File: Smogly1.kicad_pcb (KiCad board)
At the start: 2 copper layers, 93.2 x 68 mm, 9 parts, among them J1 VCC IN, J10 NodeMCU A0-VIN, J11 NodeMCU D0-3.3V, J2 PMSx003, J3 BME280, J4 microUSB, J5 5/3.3/GND, J6 DeepSleep, J8 D5/6/7/8

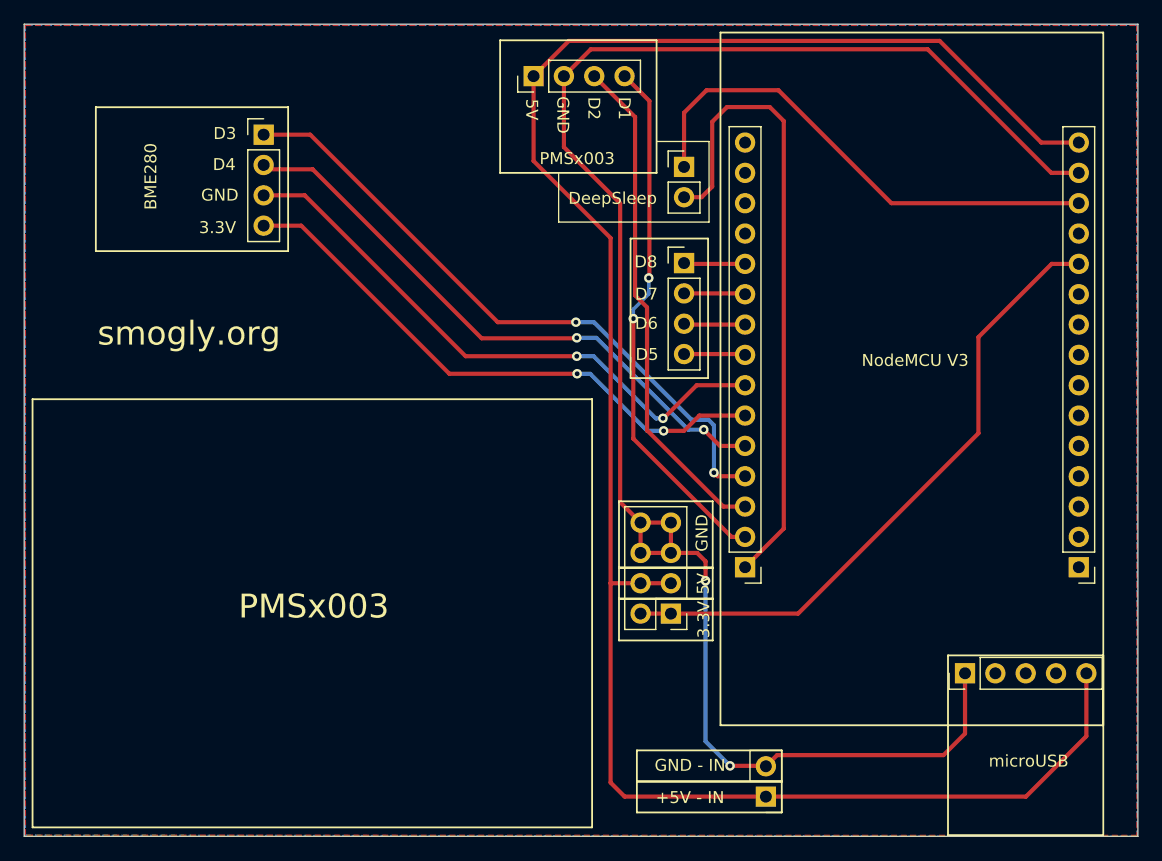
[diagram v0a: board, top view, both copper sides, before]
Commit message: added PMS7003 connector
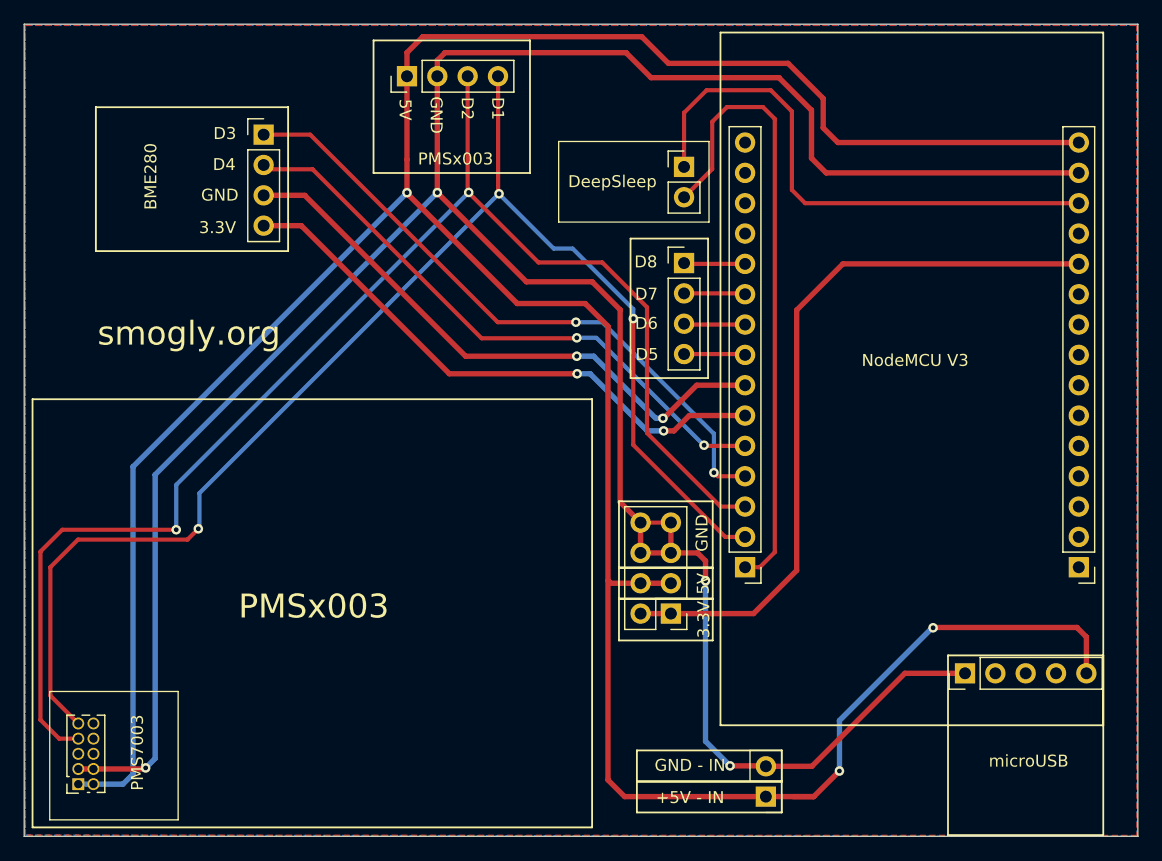
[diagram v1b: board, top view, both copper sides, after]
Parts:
- added J9: PMS7003_Conn, Connector_PinSocket_1.27mm:PinSocket_2x05_P1.27mm_Vertical, F.Cu at (169.5, 132.1)
- moved J2 10.6 mm to (197.0, 72.8)
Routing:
- net +5V: track 165.0 -> 255.8 mm, vias 0 -> 3
- net GND: track 145.6 -> 228.4 mm, vias 2 -> 4
- net Net-(J11-Pad3): track 42.3 -> 118.4 mm, vias 0 -> 2
- net Net-(J11-Pad2): track 44.5 -> 115.3 mm, vias 2 -> 3
- net +3V3: track 53.5 -> 61.6 mm
- net Net-(J10-Pad13): track 42.3 -> 46.1 mm
- net Net-(J11-Pad1): track 53.8 -> 52.7 mm
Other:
- board text added: "PMS7003"

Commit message: 11.05.2021
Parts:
- moved J10 2.00 mm to (253.2, 115.9)
- moved J11 2.00 mm to (225.3, 115.9)
- moved J9 1.12 mm to (170.0, 131.1)
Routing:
- net Net-(J10-Pad13): track 46.1 -> 39.2 mm
- net Net-(J11-Pad2): track 115.3 -> 111.7 mm
- net Net-(J11-Pad3): track 118.4 -> 115.2 mm
- net Net-(J11-Pad1): track 52.7 -> 49.8 mm
- net GND: track 228.4 -> 225.5 mm, vias 4 -> 32
- net +5V: track 255.8 -> 253.3 mm, vias 3 -> 4
- net Net-(J11-Pad4): track 54.1 -> 55.9 mm
- net Net-(J11-Pad5): track 49.9 -> 51.0 mm
- net Net-(J11-Pad9): track 5.14 -> 6.17 mm
- net Net-(J11-Pad11): track 5.14 -> 6.17 mm
- net +3V3: track 61.6 -> 60.8 mm
- net Net-(J11-Pad8): track 5.14 -> 5.97 mm
- net Net-(J11-Pad10): track 5.14 -> 5.97 mm
- net Net-(J11-Pad7): track 49.2 -> 48.4 mm
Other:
- board size 93.2 x 68 mm -> 92.2 x 68 mm
- board text added: "antena"

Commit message: 11.05.2021
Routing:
- net GND: track 225.5 -> 224.4 mm
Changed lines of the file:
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@@
   (segment (start 177.68 109.85) (end 177.68 107.02) (width 0.35) (layer "B.Cu") (net 2))
   (segment (start 214.04 115.26) (end 214.04 115.24) (width 0.45) (layer "F.Cu") (net 3))
+  (segment (start 197 70.83) (end 197 72.81) (width 0.45) (layer "F.Cu") (net 3))
   (segment (start 197 79.78) (end 197 79.91338) (width 0.35) (layer "F.Cu") (net 3))
-  (segment (start 233.3 80.36) (end 227.58 74.64) (width 0.45) (layer "F.Cu") (net 3))
-  (segment (start 216.004519 70.135481) (end 197.69452 70.13548) (width 0.45) (layer "F.Cu") (net 3))
-  (segment (start 253.25 80.36) (end 233.3 80.36) (width 0.45) (layer "F.Cu") (net 3))
   (segment (start 213.46 131.36) (end 215.225 133.125) (width 0.45) (layer "F.Cu") (net 3))
   (segment (start 169.99 131.09) (end 173.28 131.09) (width 0.45) (layer "F.Cu") (net 3))
+  (segment (start 197.69452 70.13548) (end 197 70.83) (width 0.45) (layer "F.Cu") (net 3))
   (segment (start 231.065 133.125) (end 227.05 133.125) (width 0.45) (layer "F.Cu") (net 3))
   (segment (start 169.98 131.08) (end 169.99 131.09) (width 0.45) (layer "F.Cu") (net 3))
   (segment (start 233.21 130.98) (end 231.065 133.125) (width 0.45) (layer "F.Cu") (net 3))
   (segment (start 206.23 91.84) (end 211.93 91.84) (width 0.45) (layer "F.Cu") (net 3))
-  (segment (start 197 70.83) (end 197 72.81) (width 0.45) (layer "F.Cu") (net 3))
   (segment (start 219.1 115.26) (end 216.56 115.26) (width 0.45) (layer "F.Cu") (net 3))
   (segment (start 214.04 115.24) (end 213.83 115.03) (width 0.45) (layer "F.Cu") (net 3))
   (segment (start 241.05 118.99) (end 241.08 118.96) (width 0.45) (layer "F.Cu") (net 3))
+  (segment (start 233.3 80.36) (end 227.58 74.64) (width 0.45) (layer "F.Cu") (net 3))
+  (segment (start 215.34548 70.13548) (end 197.69452 70.13548) (width 0.45) (layer "F.Cu") (net 3))
   (segment (start 231.065 133.125) (end 229.315 133.125) (width 0.45) (layer "F.Cu") (net 3))
   (segment (start 213.46 93.37) (end 213.46 131.36) (width 0.45) (layer "F.Cu") (net 3))
   (segment (start 216.56 115.26) (end 214.04 115.26) (width 0.45) (layer "F.Cu") (net 3))
+  (segment (start 219.85 74.64) (end 215.34548 70.13548) (width 0.45) (layer "F.Cu") (net 3))
   (segment (start 253.09 118.96) (end 253.885 119.755) (width 0.45) (layer "F.Cu") (net 3))
   (segment (start 197 82.56) (end 197 82.61) (width 0.45) (layer "F.Cu") (net 3))
@@
   (segment (start 197 82.61) (end 206.23 91.84) (width 0.45) (layer "F.Cu") (net 3))
   (segment (start 211.93 91.84) (end 213.46 93.37) (width 0.45) (layer "F.Cu") (net 3))
-  (segment (start 227.58 74.64) (end 220.509038 74.64) (width 0.45) (layer "F.Cu") (net 3))
   (segment (start 241.08 118.96) (end 253.09 118.96) (width 0.45) (layer "F.Cu") (net 3))
   (segment (start 215.225 133.125) (end 227.05 133.125) (width 0.45) (layer "F.Cu") (net 3))
-  (segment (start 197.69452 70.13548) (end 197 70.83) (width 0.45) (layer "F.Cu") (net 3))
   (segment (start 197 79.78) (end 197 82.56) (width 0.45) (layer "F.Cu") (net 3))
+  (segment (start 253.25 80.36) (end 233.3 80.36) (width 0.45) (layer "F.Cu") (net 3))
   (segment (start 197 72.81) (end 197 79.78) (width 0.45) (layer "F.Cu") (net 3))
-  (segment (start 220.509038 74.64) (end 216.004519 70.135481) (width 0.45) (layer "F.Cu") (net 3))
+  (segment (start 227.58 74.64) (end 219.85 74.64) (width 0.45) (layer "F.Cu") (net 3))
   (via (at 233.21 130.98) (size 0.8) (drill 0.4) (layers "F.Cu" "B.Cu") (net 3))
   (via (at 173.28 131.09) (size 0.8) (drill 0.4) (layers "F.Cu" "B.Cu") (net 3))
@@
   (segment (start 174.06 105.5) (end 174.06 130.31) (width 0.45) (layer "B.Cu") (net 3))
   (segment (start 199.54 82.56) (end 207 90.02) (width 0.45) (layer "F.Cu") (net 4))
+  (segment (start 234.7 82.9) (end 227.26 75.46) (width 0.45) (layer "F.Cu") (net 4))
   (segment (start 199.54 72.81) (end 199.54 82.55) (width 0.45) (layer "F.Cu") (net 4))
+  (segment (start 219.04 75.46) (end 214.83 71.25) (width 0.45) (layer "F.Cu") (net 4))
   (segment (start 216.56 110.18) (end 219.1 110.18) (width 0.35) (layer "F.Cu") (net 4))
   (segment (start 199.54 82.55) (end 199.54 82.56) (width 0.45) (layer "F.Cu") (net 4))
@@
   (segment (start 214.73 108.35) (end 216.56 110.18) (width 0.45) (layer "F.Cu") (net 4))
   (segment (start 230.905 130.585) (end 227.05 130.585) (width 0.45) (layer "F.Cu") (net 4))
-  (segment (start 234.7 82.9) (end 227.26 75.46) (width 0.45) (layer "F.Cu") (net 4))
   (segment (start 216.56 112.72) (end 216.56 110.18) (width 0.45) (layer "F.Cu") (net 4))
+  (segment (start 201.1 71.25) (end 199.54 72.81) (width 0.45) (layer "F.Cu") (net 4))
+  (segment (start 214.83 71.25) (end 201.1 71.25) (width 0.45) (layer "F.Cu") (net 4))
   (segment (start 219.1 110.18) (end 219.1 112.72) (width 0.45) (layer "F.Cu") (net 4))
   (segment (start 222 113.39) (end 221.33 112.72) (width 0.45) (layer "F.Cu") (net 4))
@@
   (segment (start 221.33 112.72) (end 219.1 112.72) (width 0.45) (layer "F.Cu") (net 4))
   (segment (start 227.015 130.55) (end 227.05 130.585) (width 0.35) (layer "F.Cu") (net 4))
-  (segment (start 253.25 82.9) (end 234.7 82.9) (width 0.45) (layer "F.Cu") (net 4))
   (segment (start 224.05 130.55) (end 227.015 130.55) (width 0.45) (layer "F.Cu") (net 4))
   (segment (start 207 90.02) (end 212.51 90.02) (width 0.45) (layer "F.Cu") (net 4))
-  (segment (start 219.97 75.46) (end 215.345 70.835) (width 0.45) (layer "F.Cu") (net 4))
   (segment (start 222 115.05) (end 222 113.39) (width 0.45) (layer "F.Cu") (net 4))
   (segment (start 219.1 112.72) (end 216.56 112.72) (width 0.45) (layer "F.Cu") (net 4))
   (segment (start 243.725 122.8) (end 238.69 122.8) (width 0.45) (layer "F.Cu") (net 4))
-  (segment (start 215.345 70.835) (end 200.185 70.835) (width 0.45) (layer "F.Cu") (net 4))
-  (segment (start 200.185 70.835) (end 199.54 71.48) (width 0.45) (layer "F.Cu") (net 4))
+  (segment (start 227.26 75.46) (end 219.04 75.46) (width 0.45) (layer "F.Cu") (net 4))
+  (segment (start 253.25 82.9) (end 234.7 82.9) (width 0.45) (layer "F.Cu") (net 4))
   (segment (start 243.245 122.32) (end 243.725 122.8) (width 0.45) (layer "F.Cu") (net 4))
-  (segment (start 227.26 75.46) (end 219.97 75.46) (width 0.45) (layer "F.Cu") (net 4))
-  (segment (start 199.54 71.48) (end 199.54 72.81) (width 0.45) (layer "F.Cu") (net 4))
   (via (at 167.63 96.81) (size 0.8) (drill 0.4) (layers "F.Cu" "B.Cu") (free) (net 4))
   (via (at 222.76 92.22) (size 0.8) (drill 0.4) (layers "F.Cu" "B.Cu") (free) (net 4))
@@
     (polygon
       (pts
-        (xy 165.05 68.55)
-        (xy 257.06815 68.55038)
-        (xy 257.09315 136.37538)
-        (xy 165.05 136.35)
+        (xy 165.619994 69.3)
+        (xy 256.056212 69.300753)
+        (xy 256.081409 135.705165)
+        (xy 165.620191 135.679412)
       )
     )
@@
     (polygon
       (pts
-        (xy 165.05 136.35)
-        (xy 257.094086 136.45038)
-        (xy 257.069086 68.55038)
-        (xy 165.05 68.55)
+        (xy 165.620801 135.631106)
+        (xy 256.083058 135.731858)
+        (xy 256.057251 69.300799)
+        (xy 165.619994 69.300047)
       )
     )

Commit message: 12.05.2021
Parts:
- moved J10 45.5 mm to (225.3, 80.0), turned to 0 degrees
- moved J11 45.5 mm to (253.2, 80.0), turned to 0 degrees
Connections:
- J4 pad 1: GND -> +5V
- J4 pad 5: +5V -> GND
- J9 pad 10: unconnected-(J9-Pad10) -> (no net)
- J9 pad 5: unconnected-(J9-Pad5) -> (no net)
- J9 pad 6: unconnected-(J9-Pad6) -> (no net)
- J9 pad 8: unconnected-(J9-Pad8) -> (no net)
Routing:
- net Net-(J11-Pad8): track 5.97 -> 85.4 mm
- net +5V: track 253.3 -> 178.1 mm, vias 4 -> 2
- net Net-(J11-Pad9): track 6.17 -> 80.8 mm
- net Net-(J11-Pad10): track 5.97 -> 77.0 mm
- net Net-(J11-Pad11): track 6.17 -> 73.6 mm
- net GND: track 224.4 -> 178.2 mm, vias 32 -> 40
- net Net-(J11-Pad6): track 47.7 -> 86.0 mm, vias 2 -> 1
- net Net-(J11-Pad7): track 48.4 -> 85.7 mm, vias 2 -> 1
- net +3V3: track 60.8 -> 23.7 mm, vias 0 -> 1
- net Net-(J11-Pad5): track 51.0 -> 85.1 mm, vias 2 -> 1
- net Net-(J11-Pad4): track 55.9 -> 84.6 mm, vias 2 -> 1
- net Net-(J11-Pad3): track 115.2 -> 137.1 mm, vias 2 -> 3
- net Net-(J11-Pad2): track 111.7 -> 129.7 mm, vias 3 -> 2
- net Net-(J11-Pad1): track 49.8 -> 43.1 mm, vias 0 -> 2
- net Net-(J10-Pad13): track 39.2 -> 43.9 mm

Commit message: KiCad 6.0
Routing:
- net Net-(J11-Pad8): track 85.4 -> 87.4 mm
- net Net-(J11-Pad9): track 80.8 -> 82.3 mm
- net Net-(J11-Pad10): track 77.0 -> 78.3 mm
- net Net-(J11-Pad11): track 73.6 -> 74.2 mm
- net Net-(J11-Pad4): track 84.6 -> 85.2 mm

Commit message: ESP32 init
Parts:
- removed J6: DeepSleep, Connector_PinHeader_2.54mm:PinHeader_1x02_P2.54mm_Vertical
- J10: value NodeMCU A0-VIN -> ESP32-DevKit VIN-EN
- J11: value NodeMCU D0-3.3V -> ESP32-DevKit 3V3-D23
- J8: value D5/6/7/8 -> D33/32/35/35
- moved J11 2.75 mm to (250.5, 80.0)
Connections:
- J10 pad 1: (no net) -> unconnected-(J10-Pad1)
- J10 pad 10: (no net) -> unconnected-(J10-Pad10)
- J10 pad 11: +3V3 -> unconnected-(J10-Pad11)
- J10 pad 12: (no net) -> unconnected-(J10-Pad12)
- J10 pad 13: Net-(J10-Pad13) -> unconnected-(J10-Pad13)
- J10 pad 2: (no net) -> unconnected-(J10-Pad2)
- J10 pad 3: (no net) -> unconnected-(J10-Pad3)
- J10 pad 4: (no net) -> Net-(J10-Pad4)
- J10 pad 5: (no net) -> Net-(J10-Pad5)
- J10 pad 6: (no net) -> Net-(J10-Pad6)
- J10 pad 7: (no net) -> Net-(J10-Pad7)
- J10 pad 8: (no net) -> unconnected-(J10-Pad8)
- J10 pad 9: (no net) -> unconnected-(J10-Pad9)
- J11 pad 10: Net-(J11-Pad10) -> unconnected-(J11-Pad10)
- J11 pad 11: Net-(J11-Pad11) -> unconnected-(J11-Pad11)
- J11 pad 12: (no net) -> unconnected-(J11-Pad12)
- J11 pad 13: (no net) -> unconnected-(J11-Pad13)
- J11 pad 14: (no net) -> Net-(J11-Pad14)
- J11 pad 15: (no net) -> +3V3
- J11 pad 3: Net-(J11-Pad3) -> unconnected-(J11-Pad3)
- J11 pad 4: Net-(J11-Pad4) -> unconnected-(J11-Pad4)
- J11 pad 5: Net-(J11-Pad5) -> unconnected-(J11-Pad5)
- J11 pad 8: Net-(J11-Pad8) -> unconnected-(J11-Pad8)
- J11 pad 9: Net-(J11-Pad9) -> unconnected-(J11-Pad9)
- J2 pad 3: Net-(J11-Pad3) -> Net-(J11-Pad2)
- J2 pad 4: Net-(J11-Pad2) -> Net-(J11-Pad1)
- J3 pad 1: Net-(J11-Pad4) -> Net-(J11-Pad6)
- J3 pad 2: Net-(J11-Pad5) -> Net-(J11-Pad7)
- J3 pad 3: Net-(J11-Pad7) -> +3V3
- J3 pad 4: Net-(J11-Pad6) -> Net-(J11-Pad14)
- J4 pad 2: (no net) -> unconnected-(J4-Pad2)
- J4 pad 3: (no net) -> unconnected-(J4-Pad3)
- J4 pad 4: (no net) -> unconnected-(J4-Pad4)
- J8 pad 1: Net-(J11-Pad11) -> Net-(J10-Pad4)
- J8 pad 2: Net-(J11-Pad10) -> Net-(J10-Pad5)
- J8 pad 3: Net-(J11-Pad9) -> Net-(J10-Pad6)
- J8 pad 4: Net-(J11-Pad8) -> Net-(J10-Pad7)
- J9 pad 10: (no net) -> unconnected-(J9-Pad10)
- J9 pad 5: (no net) -> unconnected-(J9-Pad5)
- J9 pad 6: (no net) -> unconnected-(J9-Pad6)
- J9 pad 7: Net-(J11-Pad3) -> Net-(J11-Pad2)
- J9 pad 8: (no net) -> unconnected-(J9-Pad8)
- J9 pad 9: Net-(J11-Pad2) -> Net-(J11-Pad1)
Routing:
- net Net-(J11-Pad3): track 137.1 -> 0.00 mm, vias 3 -> 0
- net +3V3: track 23.7 -> 126.5 mm, vias 1 -> 2
- net Net-(J11-Pad14): track 0.00 -> 100.4 mm, vias 0 -> 1
- net Net-(J11-Pad8): track 87.4 -> 0.00 mm
- net Net-(J11-Pad4): track 85.2 -> 0.00 mm, vias 1 -> 0
- net Net-(J11-Pad5): track 85.1 -> 0.00 mm, vias 1 -> 0
- net Net-(J11-Pad1): track 42.9 -> 125.8 mm
- net Net-(J11-Pad9): track 82.3 -> 0.00 mm
- net Net-(J11-Pad10): track 78.3 -> 0.00 mm
- net Net-(J11-Pad11): track 74.2 -> 0.00 mm
- net Net-(J10-Pad13): track 43.9 -> 0.00 mm
- net Net-(J10-Pad7): track 0.00 -> 5.45 mm
- net Net-(J10-Pad6): track 0.00 -> 5.45 mm
- net Net-(J10-Pad5): track 0.00 -> 5.45 mm
- net Net-(J10-Pad4): track 0.00 -> 5.45 mm
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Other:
- board text added: "D18"
- board text added: "D19"
- board text added: "D22"
- board text added: "D23"
- board text added: "D32"
- board text added: "D33"
- board text added: "D34"
- board text added: "D35"
- board text added: "ESP32-DevKit"
- board text removed: "D1"
- board text removed: "D2"
- board text removed: "D3"
- board text removed: "D4"
- board text removed: "D5"
- board text removed: "D6"
- board text removed: "D7"
- board text removed: "D8"
- board text removed: "DeepSleep"
- board text removed: "NodeMCU V3"
